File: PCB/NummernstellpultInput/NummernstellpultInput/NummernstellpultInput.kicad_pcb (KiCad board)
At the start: 2 copper layers, 89 x 95 mm, 48 parts, among them J1 Screw_Terminal_01x05, SW0 SW_Push, SW1 SW_Push, SW2 SW_Push, SW3 SW_Push, SW4 SW_Push, SW5 SW_Push, SW6 SW_Push, SW7 SW_Push, SW8 SW_Push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

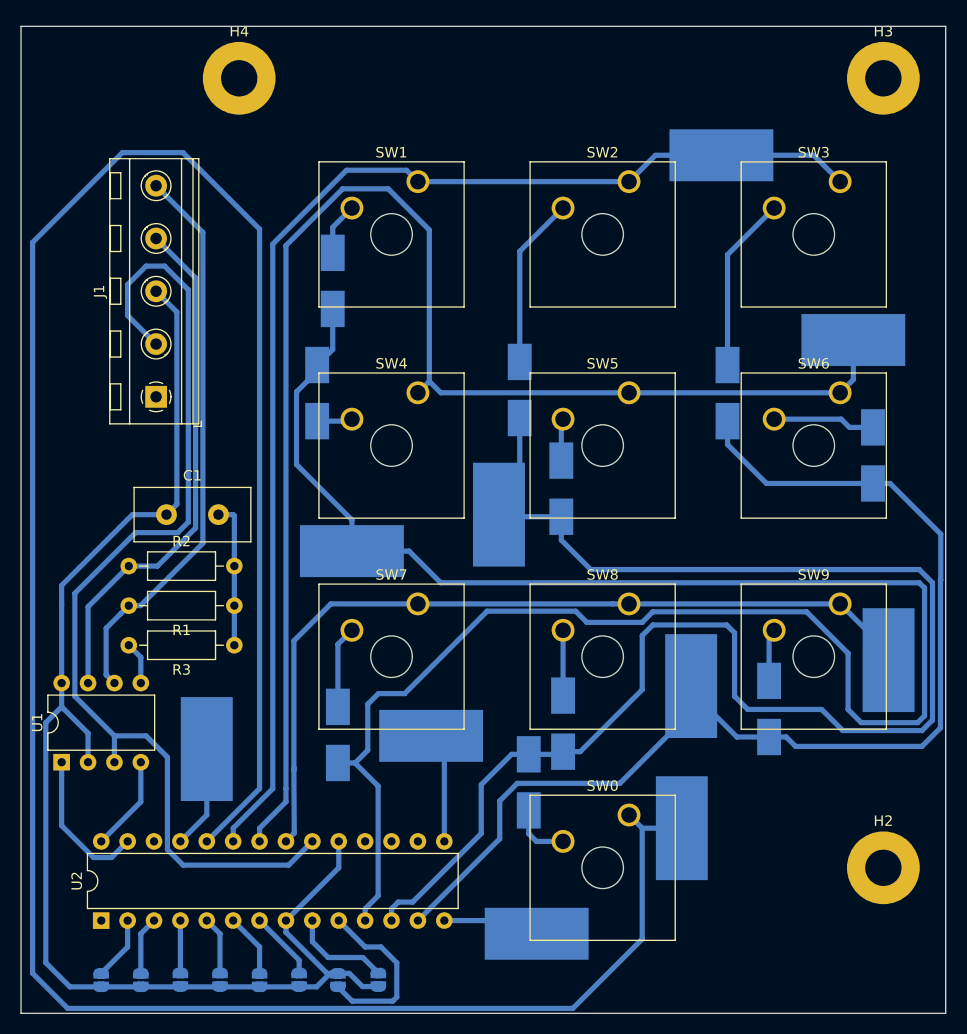
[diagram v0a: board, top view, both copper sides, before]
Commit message: Update PCBs and add track occupation PCB.
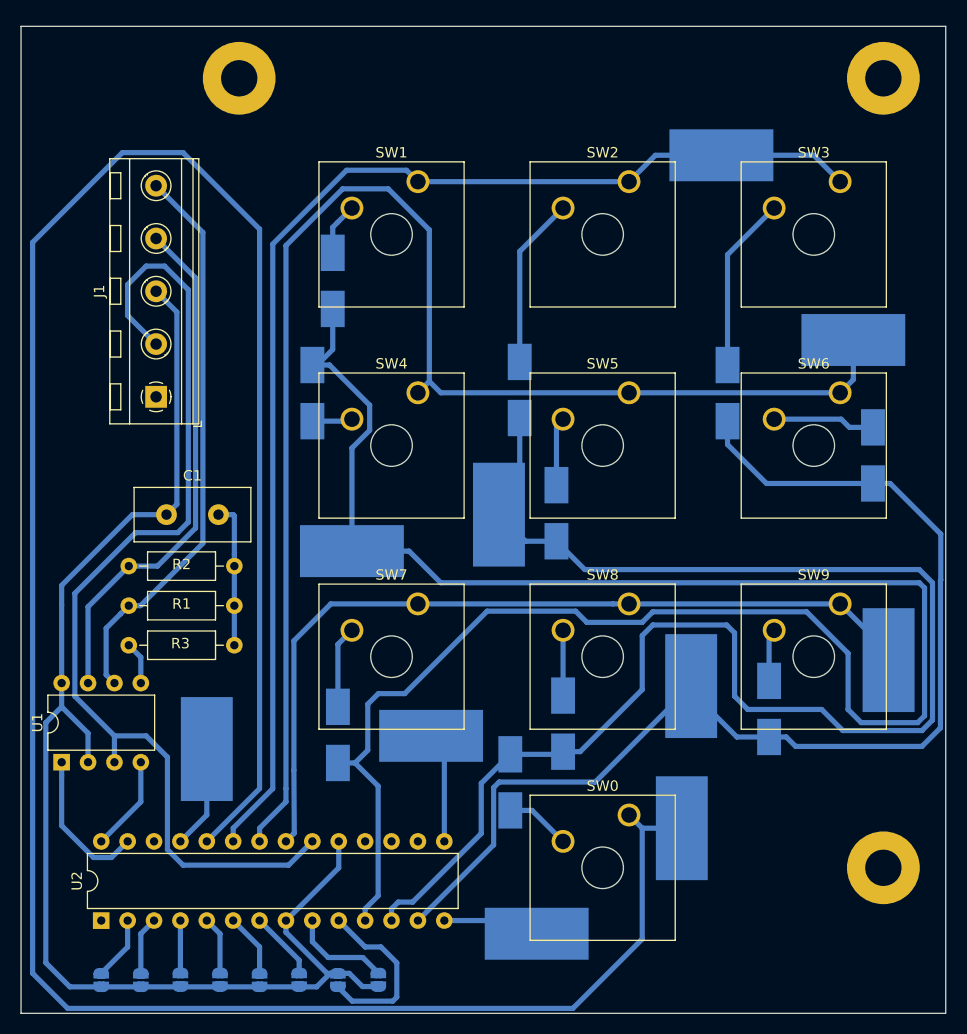
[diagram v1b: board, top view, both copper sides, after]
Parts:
- moved D5 2.41 mm to (216.5, 76.4)
- moved D7 1.78 mm to (212.1, 102.3)
- moved D2 0.46 mm to (193.0, 64.8)
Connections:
- J1 pad 1: Net-(J1-Pad1) -> unconnected-(J1-Pin_1-Pad1)
- U2 pad 1: Net-(U2-Pad1) -> unconnected-(U2-VPP/~{MCLR}/RE3-Pad1)
- U2 pad 16: Net-(U2-Pad16) -> unconnected-(U2-RC5-Pad16)
- U2 pad 17: Net-(U2-Pad17) -> unconnected-(U2-RC6-Pad17)
- U2 pad 18: Net-(U2-Pad18) -> unconnected-(U2-RC7-Pad18)
- U2 pad 26: Net-(U2-Pad26) -> unconnected-(U2-RB5-Pad26)
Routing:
- net Net-(D5-K): track 4.06 -> 6.61 mm
- net Net-(Col1-Pin_1): track 186.3 -> 187.8 mm
- net Net-(Col2-Pin_1): track 147.6 -> 146.4 mm
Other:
- net class Default removed
